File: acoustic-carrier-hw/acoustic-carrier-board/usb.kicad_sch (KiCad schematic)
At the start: 17 parts, among them J6 TYPE-C-31-M-12, Q1 SI2301CDS-T1-GE3, U6 CH340N

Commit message: [carrier] Reorganized carrier board schematic, added lcsc part numbers (next) check schematic before component placement
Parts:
- C119: footprint Capacitor_SMD:C_1206_3216Metric -> Capacitor_SMD:C_0805_2012Metric; LCSC Part Number C1848 -> (none); LPN (none) -> C28323; MPN (none) -> CL21B105KBFNNNE
- D7: LCSC Part Number C12333 -> (none); LPN (none) -> C12333
- J6: LCSC Part Number C165948 -> (none); LPN (none) -> C165948
- R49, R52: LCSC Part Number C4216 -> (none); LPN (none) -> C4216
- R53: LCSC Part Number C4125 -> (none); LPN (none) -> C4125
- R57, R58: LCSC Part Number C27834 -> (none); LPN (none) -> C27834
- U6: LPN (none) -> C2977777; MPN (none) -> CH340N
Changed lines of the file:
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@@
 			)
 		)
-		(property "LCSC Part Number" "C4216"
+		(property "LCSC Part Number" ""
 			(at 180.34 74.93 0)
 			(effects
@@
 		)
 		(property "jlcpcb" ""
+			(at 180.34 74.93 0)
+			(effects
+				(font
+					(size 1.27 1.27)
+				)
+				(hide yes)
+			)
+		)
+		(property "LPN" "C4216"
 			(at 180.34 74.93 0)
 			(effects
@@
 			)
 		)
-		(property "LCSC Part Number" "C4216"
+		(property "LCSC Part Number" ""
 			(at 180.34 86.36 0)
 			(effects
@@
 		)
 		(property "jlcpcb" ""
+			(at 180.34 86.36 0)
+			(effects
+				(font
+					(size 1.27 1.27)
+				)
+				(hide yes)
+			)
+		)
+		(property "LPN" "C4216"
 			(at 180.34 86.36 0)
 			(effects
@@
 			)
 		)
-		(property "LCSC Part Number" "C165948"
+		(property "LCSC Part Number" ""
 			(at 228.6 55.88 0)
 			(effects
@@
 		)
 		(property "jlcpcb" ""
+			(at 228.6 55.88 0)
+			(effects
+				(font
+					(size 1.27 1.27)
+				)
+				(hide yes)
+			)
+		)
+		(property "LPN" "C165948"
 			(at 228.6 55.88 0)
 			(effects
@@
 			)
 		)
-		(property "Footprint" "Capacitor_SMD:C_1206_3216Metric"
+		(property "Footprint" "Capacitor_SMD:C_0805_2012Metric"
 			(at 165.1 74.93 0)
 			(effects
@@
 			)
 		)
-		(property "Datasheet" "https://wmsc.lcsc.com/wmsc/upload/file/pdf/v2/lcsc/2304140030_Samsung-Electro-Mechanics-CL31B105KBHNNNE_C1848.pdf"
+		(property "Datasheet" "https://jlcpcb.com/api/file/downloadByFileSystemAccessId/8579706862004473856"
 			(at 165.1 74.93 0)
 			(effects
@@
 			)
 		)
-		(property "LCSC Part Number" "C1848"
+		(property "LCSC Part Number" ""
 			(at 165.1 74.93 0)
 			(effects
@@
 		)
 		(property "jlcpcb" ""
+			(at 165.1 74.93 0)
+			(effects
+				(font
+					(size 1.27 1.27)
+				)
+				(hide yes)
+			)
+		)
+		(property "LPN" "C28323"
+			(at 165.1 74.93 0)
+			(effects
+				(font
+					(size 1.27 1.27)
+				)
+				(hide yes)
+			)
+		)
+		(property "MPN" "CL21B105KBFNNNE"
 			(at 165.1 74.93 0)
 			(effects
@@
 			)
 		)
+		(property "LPN" "C2977777"
+			(at 106.68 44.45 0)
+			(effects
+				(font
+					(size 1.27 1.27)
+				)
+				(hide yes)
+			)
+		)
+		(property "MPN" "CH340N"
+			(at 106.68 44.45 0)
+			(effects
+				(font
+					(size 1.27 1.27)
+				)
+				(hide yes)
+			)
+		)
 		(pin "3"
 		)
@@
 			)
 		)
-		(property "LCSC Part Number" "C4125"
+		(property "LCSC Part Number" ""
 			(at 201.93 44.45 0)
 			(effects
@@
 		)
 		(property "jlcpcb" ""
+			(at 201.93 44.45 0)
+			(effects
+				(font
+					(size 1.27 1.27)
+				)
+				(hide yes)
+			)
+		)
+		(property "LPN" "C4125"
 			(at 201.93 44.45 0)
 			(effects
@@
 			)
 		)
-		(property "LCSC Part Number" "C27834"
+		(property "LCSC Part Number" ""
 			(at 198.755 76.2 0)
 			(effects
@@
 			)
 		)
+		(property "LPN" "C27834"
+			(at 198.755 76.2 0)
+			(effects
+				(font
+					(size 1.27 1.27)
+				)
+				(hide yes)
+			)
+		)
 		(pin "2"
 		)
@@
 			)
 		)
-		(property "LCSC Part Number" "C12333"
+		(property "LCSC Part Number" ""
 			(at 163.83 53.975 0)
 			(effects
@@
 		(property "jlcpcb" ""
 			(at 163.83 53.975 0)
+			(effects
+				(font
+					(size 1.27 1.27)
+				)
+				(hide yes)
+			)
+		)
+		(property "LPN" "C12333"
+			(at 163.83 53.975 90)
 			(effects
 				(font
@@
 			)
 		)
-		(property "LCSC Part Number" "C27834"
+		(property "LCSC Part Number" ""
 			(at 206.375 76.2 0)
 			(effects
@@
 			(at 206.375 76.2 0)
 			(effects
+				(font
+					(size 1.27 1.27)
+				)
+				(hide yes)
+			)
+		)
+		(property "LPN" "C27834"
+			(at 206.375 76.2 0)
+			(effects

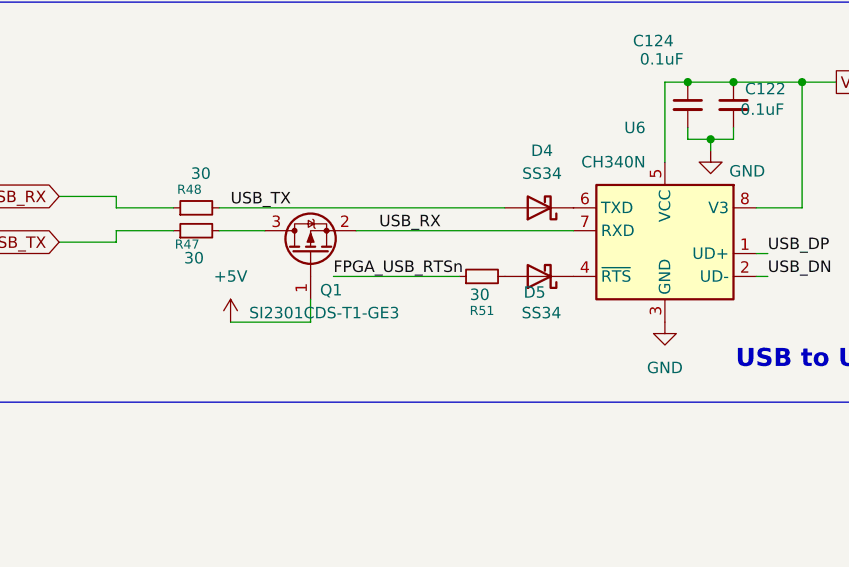
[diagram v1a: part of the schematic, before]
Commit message: [carrier] Started schematic check, replaced 8 with 16 pin connectors
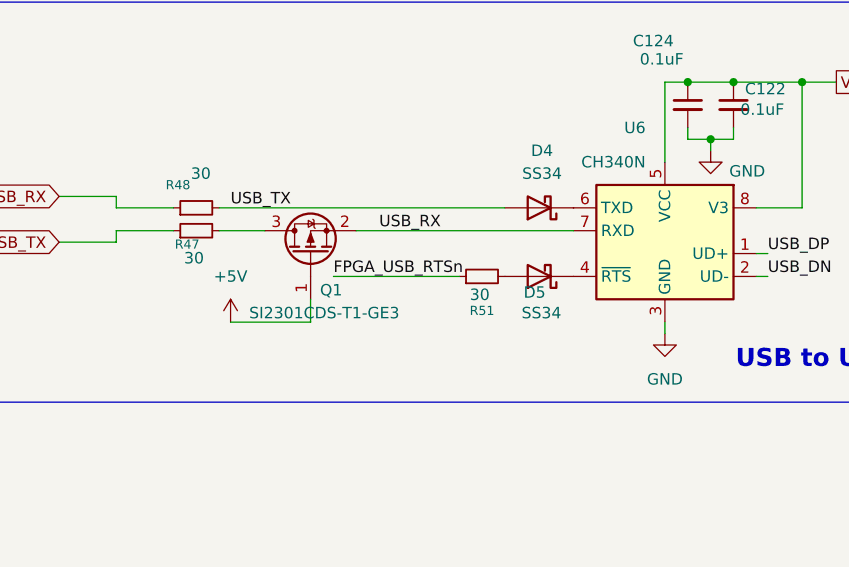
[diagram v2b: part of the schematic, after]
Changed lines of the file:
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@@
+	(wire
+		(pts
+			(xy 106.68 55.88) (xy 106.68 54.61)
+		)
+		(stroke
+			(width 0)
+			(type default)
+		)
+	)
 	(wire
 		(pts
@@
 	)
 	(symbol
-		(lib_id "power:GND")
-		(at 106.68 54.61 0)
-		(mirror y)
-		(unit 1)
-		(exclude_from_sim no)
-		(in_bom yes)
-		(on_board yes)
-		(dnp no)
-		(fields_autoplaced yes)
-		(property "Reference" "#PWR079"
-			(at 106.68 60.96 0)
-			(effects
-				(font
-					(size 1.27 1.27)
-				)
-				(hide yes)
-			)
-		)
-		(property "Value" "GND"
-			(at 106.68 59.69 0)
-			(effects
-				(font
-					(size 1.27 1.27)
-				)
-			)
-		)
-		(property "Footprint" ""
-			(at 106.68 54.61 0)
-			(effects
-				(font
-					(size 1.27 1.27)
-				)
-				(hide yes)
-			)
-		)
-		(property "Datasheet" ""
-			(at 106.68 54.61 0)
-			(effects
-				(font
-					(size 1.27 1.27)
-				)
-				(hide yes)
-			)
-		)
-		(property "Description" "Power symbol creates a global label with name \"GND\" , ground"
-			(at 106.68 54.61 0)
-			(effects
-				(font
-					(size 1.27 1.27)
-				)
-				(hide yes)
-			)
-		)
-		(pin "1"
-		)
-		(instances
-			(project "acoustic-carrier-board"
-				(path "/25b015c9-ab13-4427-b72c-b6f348597100/d85f0c18-d011-408e-9192-d89f0585c7ff/025b04a2-9f2c-45e9-92b2-e4ddadbf32dd"
-					(reference "#PWR079")
-					(unit 1)
-				)
-			)
-		)
-	)
-	(symbol
 		(lib_id "Device:R_Small")
 		(at 180.34 86.36 0)
@@
 	)
 	(symbol
+		(lib_name "GND_1")
+		(lib_id "power:GND")
+		(at 106.68 55.88 0)
+		(unit 1)
+		(exclude_from_sim no)
+		(in_bom yes)
+		(on_board yes)
+		(dnp no)
+		(fields_autoplaced yes)
+		(property "Reference" "#PWR097"
+			(at 106.68 62.23 0)
+			(effects
+				(font
+					(size 1.27 1.27)
+				)
+				(hide yes)
+			)
+		)
+		(property "Value" "GND"
+			(at 106.68 60.96 0)
+			(effects
+				(font
+					(size 1.27 1.27)
+				)
+			)
+		)
+		(property "Footprint" ""
+			(at 106.68 55.88 0)
+			(effects
+				(font
+					(size 1.27 1.27)
+				)
+				(hide yes)
+			)
+		)
+		(property "Datasheet" ""
+			(at 106.68 55.88 0)
+			(effects
+				(font
+					(size 1.27 1.27)
+				)
+				(hide yes)
+			)
+		)
+		(property "Description" "Power symbol creates a global label with name \"GND\" , ground"
+			(at 106.68 55.88 0)
+			(effects
+				(font
+					(size 1.27 1.27)
+				)
+				(hide yes)
+			)
+		)
+		(pin "1"
+		)
+		(instances
+			(project ""
+				(path "/25b015c9-ab13-4427-b72c-b6f348597100/d85f0c18-d011-408e-9192-d89f0585c7ff/025b04a2-9f2c-45e9-92b2-e4ddadbf32dd"
+					(reference "#PWR097")
+					(unit 1)
+				)
+			)
+		)
+	)
+	(symbol
 		(lib_id "power:GND")
 		(at 241.3 32.385 0)
@@
 		(dnp no)
 		(property "Reference" "R48"
-			(at 53.848 39.878 90)
-			(effects
-				(font
+			(at 52.578 39.37 90)
+			(effects
+				(font

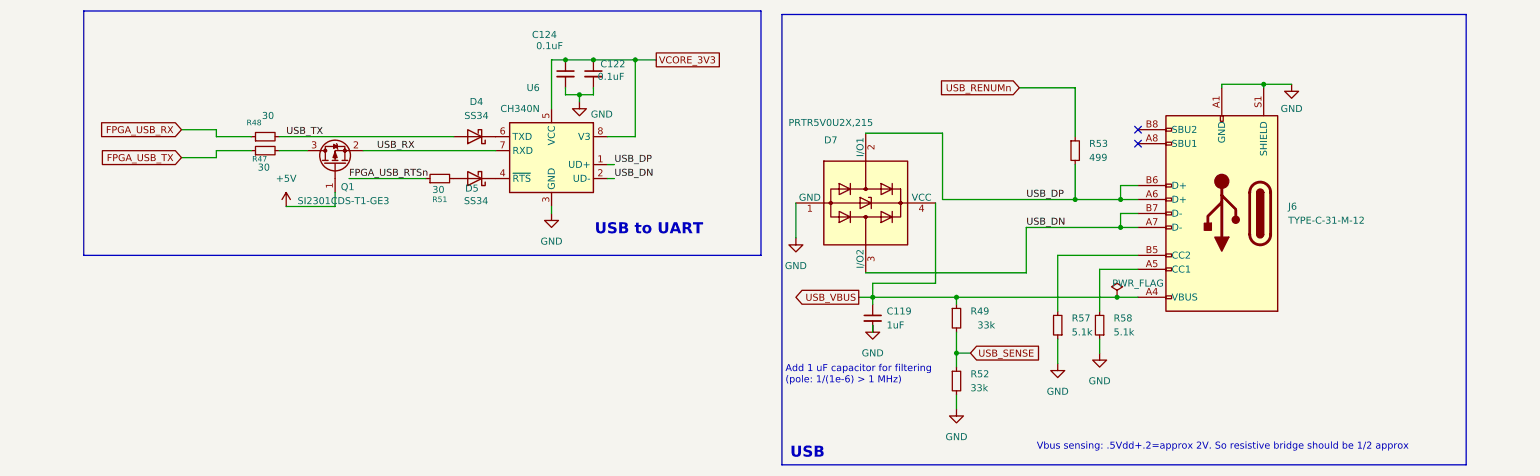
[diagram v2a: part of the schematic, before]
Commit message: [carrier] Fixed most of the carrier board ERC issues (next) fix BGA ERC issue
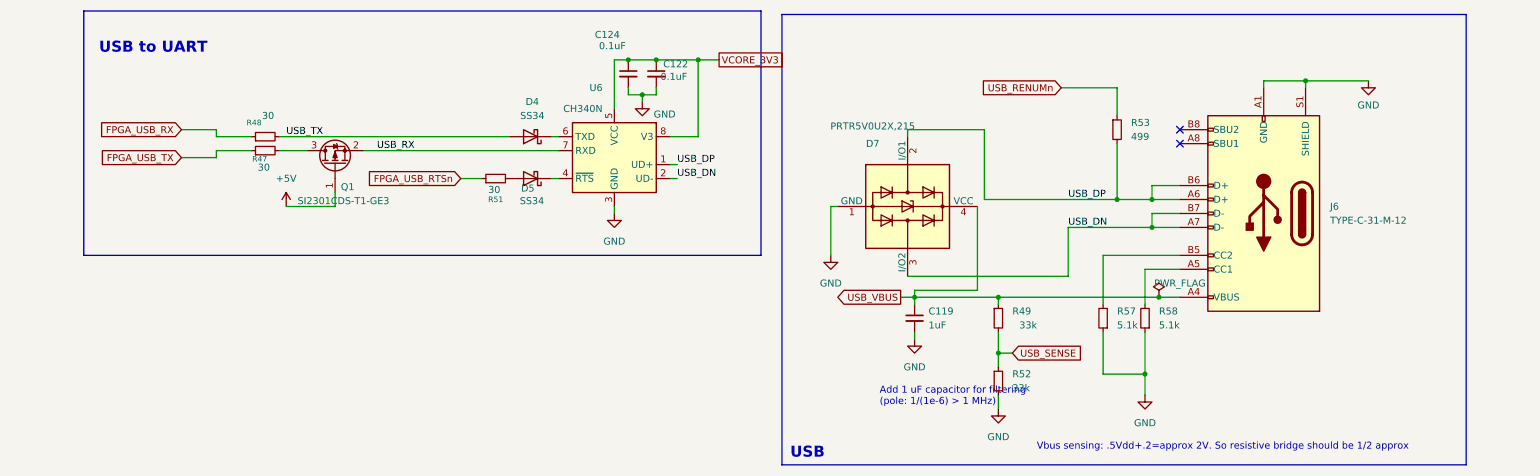
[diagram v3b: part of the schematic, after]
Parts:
- R49: MPN (none) -> 0603WAF3302T5E; Manufacturing part number 0603WAF3302T5E -> (none)
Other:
- moved on the sheet: C119, C122, C124, D4, D5, D7, J6, R49, R51, R52, R53, R57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

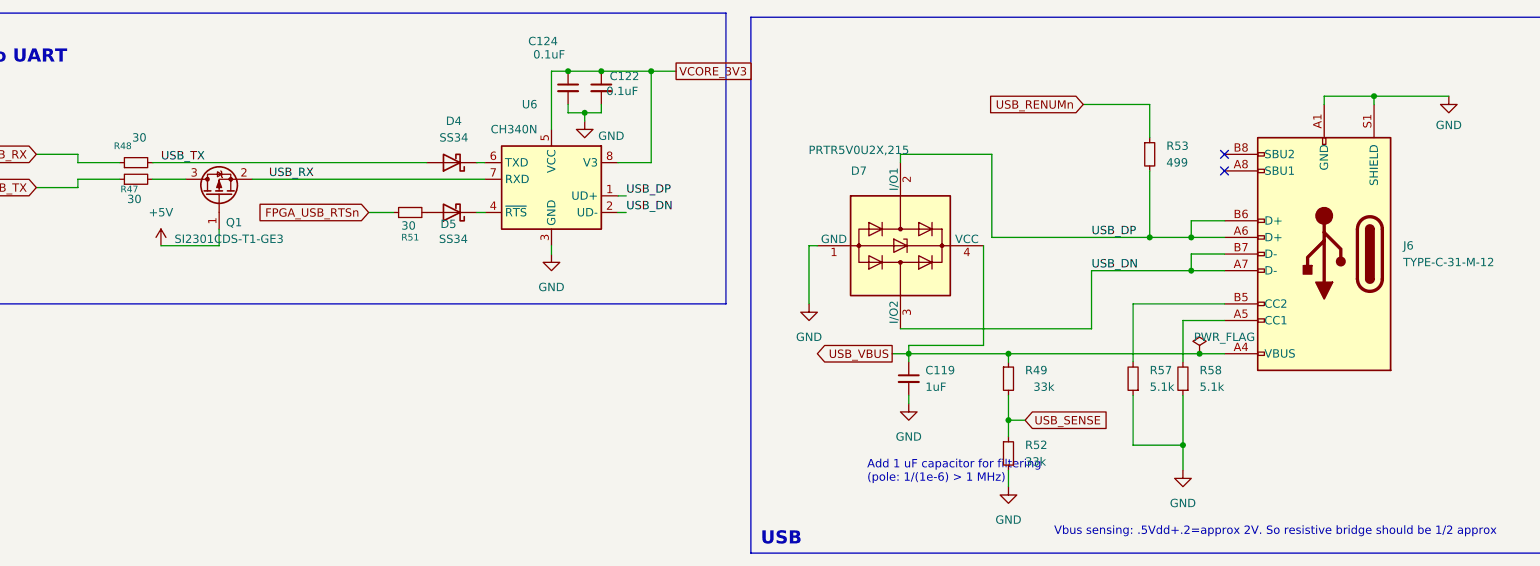
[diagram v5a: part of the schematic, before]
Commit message: [carrier] Checked ethernet decoupling + pins + pad + resonator
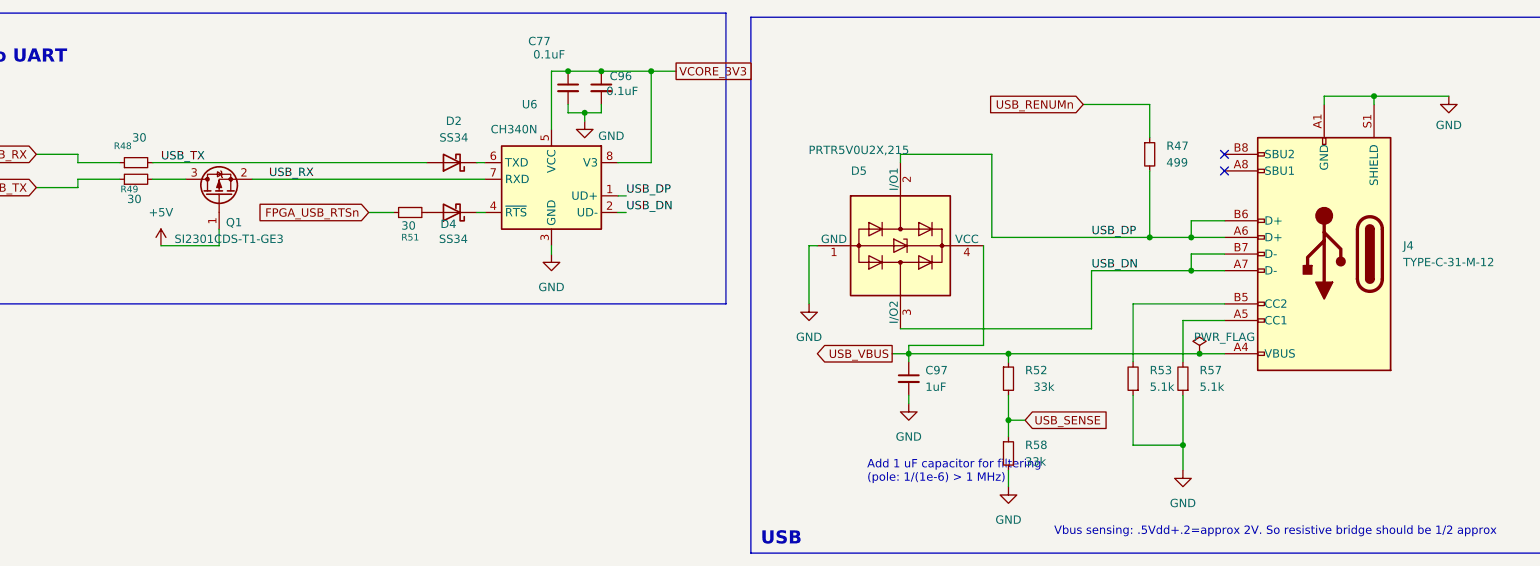
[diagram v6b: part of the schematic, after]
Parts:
- renumbered C124 to C77, C122 to C96, C119 to C97, D4 to D2, D5 to D4, D7 to D5, J6 to J4, R53 to R47, R47 to R49, R49 to R52, R57 to R53, R58 to R57, R52 to R58
